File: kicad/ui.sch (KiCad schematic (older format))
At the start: 13 parts, among them J1401 NHD-4.3-480272FT-CTXL-T, J1402 Conn_01x02, U1401 PAM8301

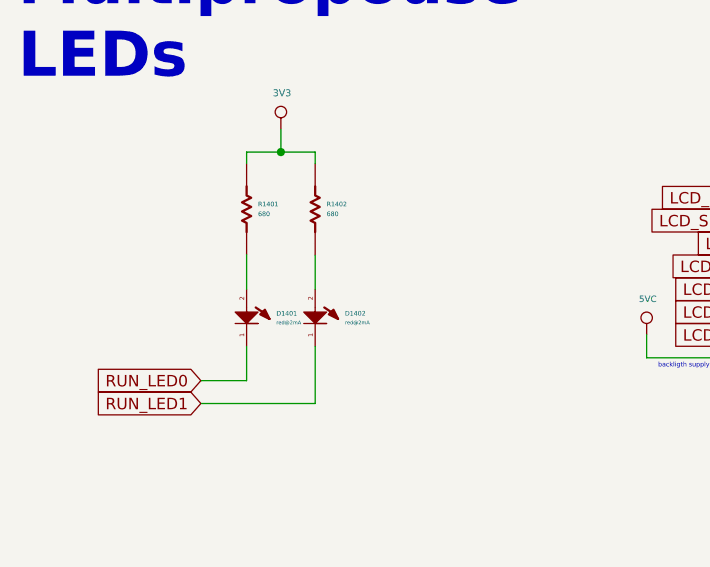
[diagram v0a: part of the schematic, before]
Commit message: making some nets space
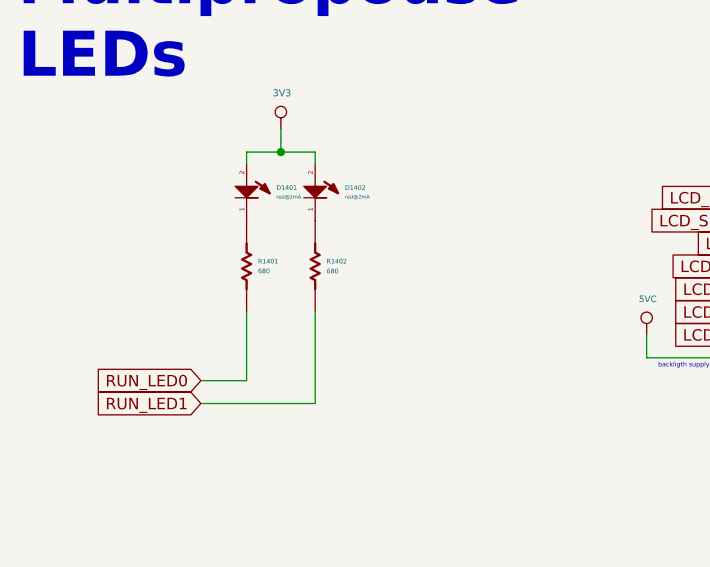
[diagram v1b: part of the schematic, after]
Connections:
- wire segments 65 -> 63
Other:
- moved on the sheet: D1401, D1402, R1401, R1402
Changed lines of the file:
@@
 	1    0    0    -1
 $EndComp
-Wire Wire Line
-	2650 2150 2650 2000
-Wire Wire Line
-	2350 2000 2350 2150
-Wire Wire Line
-	2650 2650 2650 2400
 Text Notes 1350 1250 0    197  ~ 39
 Multipropouse\nLEDs
@@
 L servo:LED_A2_K1 D?
 U 1 1 5DB38F6A
-P 2650 2250
+P 2650 1700
 AR Path="/5DD4DF4C/5DB38F6A" Ref="D?"  Part="1"
 AR Path="/5E0D58C4/5DB38F6A" Ref="D?"  Part="1"
 AR Path="/5E72D841/5DB38F6A" Ref="D1402"  Part="1"
-F 0 "D1402" V 2656 2380 20  0000 L CNN
-F 1 "red@2mA" V 2696 2380 16  0000 L CNN
-F 2 "servo:LED_0603_1608Metric" H 2450 2050 60  0001 C CNN
-F 3 "" H 2450 2050 60  0001 C CNN
-F 4 "Red" V -6350 2450 60  0001 C CNN "VALUE"
-	1    2650 2250
+F 0 "D1402" V 2656 1830 20  0000 L CNN
+F 1 "red@2mA" V 2696 1830 16  0000 L CNN
+F 2 "servo:LED_0603_1608Metric" H 2450 1500 60  0001 C CNN
+F 3 "" H 2450 1500 60  0001 C CNN
+F 4 "Red" V -6350 1900 60  0001 C CNN "VALUE"
+	1    2650 1700
 	0    1    1    0
 $EndComp
@@
 L servo:Resistor R?
 U 1 1 5DB38F5F
-P 2350 1800
+P 2350 2050
 AR Path="/5DD4DF4C/5DB38F5F" Ref="R?"  Part="1"
 AR Path="/5E0D58C4/5DB38F5F" Ref="R?"  Part="1"
 AR Path="/5E72D841/5DB38F5F" Ref="R1401"  Part="1"
-F 0 "R1401" V 2328 1850 20  0000 L CNN
-F 1 "680" V 2371 1850 20  0000 L CNN
-F 2 "Resistor_SMD:R_0603_1608Metric" H 1850 1700 60  0001 C CNN
-F 3 "" H 1950 1800 60  0001 C CNN
-F 4 "680" V -6050 2600 60  0001 C CNN "ValueDisplayed"
-	1    2350 1800
+F 0 "R1401" V 2328 2100 20  0000 L CNN
+F 1 "680" V 2371 2100 20  0000 L CNN
+F 2 "Resistor_SMD:R_0603_1608Metric" H 1850 1950 60  0001 C CNN
+F 3 "" H 1950 2050 60  0001 C CNN
+F 4 "680" V -6050 2850 60  0001 C CNN "ValueDisplayed"
+	1    2350 2050
 	0    1    1    0
 $EndComp
@@
 L servo:Resistor R?
 U 1 1 5E170B1F
-P 2650 1800
+P 2650 2050
 AR Path="/5DD4DF4C/5E170B1F" Ref="R?"  Part="1"
 AR Path="/5E0D58C4/5E170B1F" Ref="R?"  Part="1"
 AR Path="/5E72D841/5E170B1F" Ref="R1402"  Part="1"
-F 0 "R1402" V 2628 1850 20  0000 L CNN
-F 1 "680" V 2671 1850 20  0000 L CNN
-F 2 "Resistor_SMD:R_0603_1608Metric" H 2150 1700 60  0001 C CNN
-F 3 "" H 2250 1800 60  0001 C CNN
-F 4 "680" V -6350 2600 60  0001 C CNN "ValueDisplayed"
-	1    2650 1800
+F 0 "R1402" V 2628 2100 20  0000 L CNN
+F 1 "680" V 2671 2100 20  0000 L CNN
+F 2 "Resistor_SMD:R_0603_1608Metric" H 2150 1950 60  0001 C CNN
+F 3 "" H 2250 2050 60  0001 C CNN
+F 4 "680" V -6350 2850 60  0001 C CNN "ValueDisplayed"
+	1    2650 2050
 	0    1    1    0
 $EndComp
@@
 L servo:LED_A2_K1 D?
 U 1 1 5DB38F35
-P 2350 2250
+P 2350 1700
 AR Path="/5DD4DF4C/5DB38F35" Ref="D?"  Part="1"
 AR Path="/5E0D58C4/5DB38F35" Ref="D?"  Part="1"
 AR Path="/5E72D841/5DB38F35" Ref="D1401"  Part="1"
-F 0 "D1401" V 2356 2380 20  0000 L CNN
-F 1 "red@2mA" V 2396 2380 16  0000 L CNN
-F 2 "servo:LED_0603_1608Metric" H 2150 2050 60  0001 C CNN
-F 3 "" H 2150 2050 60  0001 C CNN
-F 4 "Red" V -6050 2450 60  0001 C CNN "VALUE"
-	1    2350 2250
+F 0 "D1401" V 2356 1830 20  0000 L CNN
+F 1 "red@2mA" V 2396 1830 16  0000 L CNN
+F 2 "servo:LED_0603_1608Metric" H 2150 1500 60  0001 C CNN
+F 3 "" H 2150 1500 60  0001 C CNN
+F 4 "Red" V -6050 1900 60  0001 C CNN "VALUE"
+	1    2350 1700
 	0    1    1    0
 $EndComp
@@
 Wire Wire Line
 	2500 1450 2500 1550
-Wire Wire Line
-	2350 2400 2350 2550
 $Comp
 L servo:PAM8301 U1401
@@
 Text Label 9200 1850 0    20   ~ 0
 speaker-
+Wire Wire Line
+	2650 2250 2650 2650
+Wire Wire Line
+	2350 2250 2350 2550
 $EndSCHEMATC

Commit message: change in 5v interface scenario.. remove bridges
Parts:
- removed N1401: Housing, servo:case, symbol Mechanical:Housing
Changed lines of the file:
@@
 $Descr A4 11693 8268
 encoding utf-8
-Sheet 14 19
+Sheet 14 20
 Title "clk"
 Date "2020-01-09"
@@
 Wire Wire Line
 	7900 1000 8600 1000
-$Comp
-L Mechanical:Housing N1401
-U 1 1 5E32F2AD
-P 4150 4150
-F 0 "N1401" H 4303 4184 50  0000 L CNN
-F 1 "Housing" H 4303 4093 50  0000 L CNN
-F 2 "servo:case" H 4200 4200 50  0001 C CNN
-F 3 "~" H 4200 4200 50  0001 C CNN
-	1    4150 4150
-	1    0    0    -1
-$EndComp
 Text Label 9200 1750 0    20   ~ 0
 speaker+

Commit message: serigrafia...
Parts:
- R1401, R1402, R1403, R1404: footprint Resistor_SMD:R_0603_1608Metric -> servo:R_0603_1608Metric
- U1401: footprint Package_TO_SOT_SMD:SOT-23-6 -> servo:SOT-23-6
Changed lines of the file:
@@
 F 0 "R1401" V 2328 2100 20  0000 L CNN
 F 1 "680" V 2371 2100 20  0000 L CNN
-F 2 "Resistor_SMD:R_0603_1608Metric" H 1850 1950 60  0001 C CNN
+F 2 "servo:R_0603_1608Metric" H 1850 1950 60  0001 C CNN
 F 3 "" H 1950 2050 60  0001 C CNN
 F 4 "680" V -6050 2850 60  0001 C CNN "ValueDisplayed"
@@
 F 0 "R1402" V 2628 2100 20  0000 L CNN
 F 1 "680" V 2671 2100 20  0000 L CNN
-F 2 "Resistor_SMD:R_0603_1608Metric" H 2150 1950 60  0001 C CNN
+F 2 "servo:R_0603_1608Metric" H 2150 1950 60  0001 C CNN
 F 3 "" H 2250 2050 60  0001 C CNN
 F 4 "680" V -6350 2850 60  0001 C CNN "ValueDisplayed"
@@
 F 0 "U1401" H 8800 2150 39  0000 C CNN
 F 1 "PAM8301" H 8800 2050 39  0000 C CNN
-F 2 "Package_TO_SOT_SMD:SOT-23-6" H 8600 1800 50  0001 C CNN
+F 2 "servo:SOT-23-6" H 8600 1800 50  0001 C CNN
 F 3 "https://www.diodes.com/assets/Datasheets/PAM8301.pdf" H 8600 1800 50  0001 C CNN
 	1    8600 1800
@@
 F 0 "R1403" H 7300 1815 20  0000 C CNN
 F 1 "680e" H 7300 1772 20  0000 C CNN
-F 2 "Resistor_SMD:R_0603_1608Metric" H 6800 1600 60  0001 C CNN
+F 2 "servo:R_0603_1608Metric" H 6800 1600 60  0001 C CNN
 F 3 "" H 6900 1700 60  0001 C CNN
 F 4 "680" V -1700 2500 60  0001 C CNN "ValueDisplayed"
@@
 F 0 "R1404" H 7700 1815 20  0000 C CNN
 F 1 "220e" H 7700 1772 20  0000 C CNN
-F 2 "Resistor_SMD:R_0603_1608Metric" H 7200 1600 60  0001 C CNN
+F 2 "servo:R_0603_1608Metric" H 7200 1600 60  0001 C CNN
 F 3 "" H 7300 1700 60  0001 C CNN
 F 4 "680" V -1300 2500 60  0001 C CNN "ValueDisplayed"

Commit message: improving tracks under uC
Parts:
- J1402: footprint Connector_Molex:Molex_KK-254_AE-6410-02A_1x02_P2.54mm_Vertical -> servo:Molex_KK-254_AE-6410-02A_1x02_P2.54mm_Vertical
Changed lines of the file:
@@
 F 0 "J1402" H 9580 1838 39  0000 L CNN
 F 1 "Conn_01x02" H 9580 1763 39  0000 L CNN
-F 2 "Connector_Molex:Molex_KK-254_AE-6410-02A_1x02_P2.54mm_Vertical" H 9500 1850 50  0001 C CNN
+F 2 "servo:Molex_KK-254_AE-6410-02A_1x02_P2.54mm_Vertical" H 9500 1850 50  0001 C CNN
 F 3 "~" H 9500 1850 50  0001 C CNN
 	1    9500 1850

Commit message: bom bom bom...
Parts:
- C1404: Description (none) -> CAP CER 1UF 10V X7R 0603; PartNumber (none) -> C0603C105K8RACTU; digikey (none) -> 399-11133-1-ND
- D1401: value red@2mA -> yellow@2mA; PartNumber (none) -> LY L29K-H1K2-26-Z; VALUE Red -> (none); digikey (none) -> 475-1196-1-ND
- D1402: PartNumber (none) -> LS L29K-G1H2-1-Z; VALUE Red -> (none); digikey (none) -> LS L29K-G1H2-1-Z
- R1401, R1402: value 680 -> 560; ValueDisplayed 680 -> (none)
- R1403: value 680e -> 680; ValueDisplayed 680 -> (none)
- R1404: value 220e -> 220; ValueDisplayed 680 -> (none)
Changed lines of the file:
@@
 F 1 "red@2mA" V 2696 1830 16  0000 L CNN
 F 2 "servo:LED_0603_1608Metric" H 2450 1500 60  0001 C CNN
-F 3 "" H 2450 1500 60  0001 C CNN
-F 4 "Red" V -6350 1900 60  0001 C CNN "VALUE"
+F 3 "../doc/datasheets/LS L29K.pdf" H 2450 1500 60  0001 C CNN
+F 4 "LS L29K-G1H2-1-Z " H 2650 1700 50  0001 C CNN "digikey"
+F 5 "LS L29K-G1H2-1-Z" H 0   0   50  0001 C CNN "PartNumber"
 	1    2650 1700
 	0    1    1    0
@@
 AR Path="/5E72D841/5DB38F5F" Ref="R1401"  Part="1"
 F 0 "R1401" V 2328 2100 20  0000 L CNN
-F 1 "680" V 2371 2100 20  0000 L CNN
+F 1 "560" V 2371 2100 20  0000 L CNN
 F 2 "servo:R_0603_1608Metric" H 1850 1950 60  0001 C CNN
 F 3 "" H 1950 2050 60  0001 C CNN
-F 4 "680" V -6050 2850 60  0001 C CNN "ValueDisplayed"
 	1    2350 2050
 	0    1    1    0
@@
 AR Path="/5E72D841/5E170B1F" Ref="R1402"  Part="1"
 F 0 "R1402" V 2628 2100 20  0000 L CNN
-F 1 "680" V 2671 2100 20  0000 L CNN
+F 1 "560" V 2671 2100 20  0000 L CNN
 F 2 "servo:R_0603_1608Metric" H 2150 1950 60  0001 C CNN
 F 3 "" H 2250 2050 60  0001 C CNN
-F 4 "680" V -6350 2850 60  0001 C CNN "ValueDisplayed"
 	1    2650 2050
 	0    1    1    0
@@
 AR Path="/5E0D58C4/5DB38F35" Ref="D?"  Part="1"
 AR Path="/5E72D841/5DB38F35" Ref="D1401"  Part="1"
-F 0 "D1401" V 2356 1830 20  0000 L CNN
-F 1 "red@2mA" V 2396 1830 16  0000 L CNN
+F 0 "D1401" V 2356 1622 20  0000 R CNN
+F 1 "yellow@2mA" V 2396 1622 16  0000 R CNN
 F 2 "servo:LED_0603_1608Metric" H 2150 1500 60  0001 C CNN
-F 3 "" H 2150 1500 60  0001 C CNN
-F 4 "Red" V -6050 1900 60  0001 C CNN "VALUE"
+F 3 "../doc/datasheets/LY L29K.pdf" H 2150 1500 60  0001 C CNN
+F 4 "475-1196-1-ND" H 2350 1700 50  0001 C CNN "digikey"
+F 5 "LY L29K-H1K2-26-Z " H 0   0   50  0001 C CNN "PartNumber"
 	1    2350 1700
 	0    1    1    0
@@
 AR Path="/5E72D841/5E351E31" Ref="R1403"  Part="1"
 F 0 "R1403" H 7300 1815 20  0000 C CNN
-F 1 "680e" H 7300 1772 20  0000 C CNN
+F 1 "680" H 7300 1772 20  0000 C CNN
 F 2 "servo:R_0603_1608Metric" H 6800 1600 60  0001 C CNN
 F 3 "" H 6900 1700 60  0001 C CNN
-F 4 "680" V -1700 2500 60  0001 C CNN "ValueDisplayed"
 	1    7300 1700
 	1    0    0    -1
@@
 AR Path="/5E72D841/5E352492" Ref="R1404"  Part="1"
 F 0 "R1404" H 7700 1815 20  0000 C CNN
-F 1 "220e" H 7700 1772 20  0000 C CNN
+F 1 "220" H 7700 1772 20  0000 C CNN
 F 2 "servo:R_0603_1608Metric" H 7200 1600 60  0001 C CNN
 F 3 "" H 7300 1700 60  0001 C CNN
-F 4 "680" V -1300 2500 60  0001 C CNN "ValueDisplayed"
 	1    7700 1700
 	1    0    0    -1
@@
 F 2 "servo:C_0603_1608Metric" H 8100 1600 60  0001 C CNN
 F 3 "" H 8100 1700 60  0000 C CNN
+F 4 "CAP CER 1UF 10V X7R 0603" H 0   0   50  0001 C CNN "Description"
+F 5 "" H 0   0   50  0001 C CNN "Mfr part number"
+F 6 "399-11133-1-ND" H 0   0   50  0001 C CNN "digikey"
+F 7 "C0603C105K8RACTU" H 0   0   50  0001 C CNN "PartNumber"
 	1    8100 1700
 	-1   0    0    1

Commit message: more bom...
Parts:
- C1401: Description (none) -> CAP CER 1000PF 16V X7R 0603; PartNumber (none) -> 0603B102K160CT; digikey (none) -> 1292-1378-1-ND
- C1403: value 10u -> 10uF; Description (none) -> 10µF ±20% 10V Ceramic Capacitor X5R 0603 (1608 Metric); PartNumber (none) -> GRM188R61A106ME69D; digikey (none) -> 490-10475-1-ND
- D1401: Description (none) -> LED YELLOW DIFFUSED 0603 SMD
- D1402: Description (none) -> LED RED DIFFUSED 0603 SMD
- J1401: value NHD-4.3-480272FT-CTXL-T -> idc2x10; Description (none) -> Connector Header Surface Mount 20 position 0.100\" (2.54mm); PartNumber (none) -> SBH11-NBPC-D10-SM-BK; digikey (none) -> S9188-ND; price@10 (none) -> 4.42400
- J1402: value Conn_01x02 -> header 1x2 2.54 molex; Description (none) -> Connector Header Through Hole 2 position 0.100\" (2.54mm); PartNumber (none) -> 0022232023; digikey (none) -> WM19468-ND; price@10 (none) -> 0.23100
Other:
- note added: "interfase directly using 20 wires flat cable\n for NHD-4.3-480272FT-CTXL-T newheaven LCD\nor hand wiring\nEA eDIP128B-6LWTP\nor using any paralel 8080 3v3 interfase bitbanging \nthe SPI and GPIO pins"
- note removed: "interfase directly using f20 wires flat cable\n for NHD-4.3-480272FT-CTXL-T newheaven LCD\nor hand wiring\nEA eDIP128B-6LWTP\nor using any paralel 8080 3v3 interfase bitbanging \nthe SPI and GPIO pins"
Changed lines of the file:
@@
 F 4 "LS L29K-G1H2-1-Z " H 2650 1700 50  0001 C CNN "digikey"
 F 5 "LS L29K-G1H2-1-Z" H 0   0   50  0001 C CNN "PartNumber"
+F 6 "LED RED DIFFUSED 0603 SMD " H 0   0   50  0001 C CNN "Description"
 	1    2650 1700
 	0    1    1    0
@@
 F 4 "475-1196-1-ND" H 2350 1700 50  0001 C CNN "digikey"
 F 5 "LY L29K-H1K2-26-Z " H 0   0   50  0001 C CNN "PartNumber"
+F 6 "LED YELLOW DIFFUSED 0603 SMD " H 0   0   50  0001 C CNN "Description"
 	1    2350 1700
 	0    1    1    0
@@
 F 2 "servo:C_0603_1608Metric" H 7500 1800 60  0001 C CNN
 F 3 "" H 7500 1900 60  0000 C CNN
+F 4 "CAP CER 1000PF 16V X7R 0603 " H 0   0   50  0001 C CNN "Description"
+F 5 "0603B102K160CT" H 0   0   50  0001 C CNN "PartNumber"
+F 6 "1292-1378-1-ND " H 0   0   50  0001 C CNN "digikey"
 	1    7500 1900
 	0    1    1    0
@@
 LCD UI interfase
 Text Notes 4650 3200 0    39   ~ 8
-interfase directly using f20 wires flat cable\n for NHD-4.3-480272FT-CTXL-T newheaven LCD\nor hand wiring\nEA eDIP128B-6LWTP\nor using any paralel 8080 3v3 interfase bitbanging \nthe SPI and GPIO pins
+interfase directly using 20 wires flat cable\n for NHD-4.3-480272FT-CTXL-T newheaven LCD\nor hand wiring\nEA eDIP128B-6LWTP\nor using any paralel 8080 3v3 interfase bitbanging \nthe SPI and GPIO pins
 $Comp
 L servo:5VC #PWR01405
@@
 P 5150 2050
 F 0 "J1401" H 5200 2651 50  0000 C CNN
-F 1 "NHD-4.3-480272FT-CTXL-T" H 5200 2568 39  0000 C CNN
+F 1 "idc2x10" H 5200 2568 39  0000 C CNN
 F 2 "servo:idc2x10_smd" H 5150 2050 50  0001 C CNN
 F 3 "../doc/datasheets/NHD-4.3-480272FT-CTXL-T.pdf" H 5200 2550 50  0001 C CNN
+F 4 " Connector Header Surface Mount 20 position 0.100\" (2.54mm) " H 0   0   50  0001 C CNN "Description"
+F 5 "SBH11-NBPC-D10-SM-BK" H 0   0   50  0001 C CNN "PartNumber"
+F 6 "S9188-ND" H 0   0   50  0001 C CNN "digikey"
+F 7 "4.42400" H 0   0   50  0001 C CNN "price@10"
 	1    5150 2050
 	1    0    0    -1
@@
 AR Path="/5E72D841/618DDB4B" Ref="C1403"  Part="1"
 F 0 "C1403" V 7972 1090 20  0000 R CNN
-F 1 "10u" V 7929 1090 20  0000 R CNN
+F 1 "10uF" V 7929 1090 20  0000 R CNN
 F 2 "servo:C_0603_1608Metric" H 7900 1100 60  0001 C CNN
 F 3 "" H 7900 1200 60  0000 C CNN
+F 4 "10µF ±20% 10V Ceramic Capacitor X5R 0603 (1608 Metric) " H 0   0   50  0001 C CNN "Description"
+F 5 "GRM188R61A106ME69D " H 0   0   50  0001 C CNN "PartNumber"
+F 6 "490-10475-1-ND" H 0   0   50  0001 C CNN "digikey"
 	1    7900 1200
 	0    -1   -1   0
@@
 P 9500 1850
 F 0 "J1402" H 9580 1838 39  0000 L CNN
-F 1 "Conn_01x02" H 9580 1763 39  0000 L CNN
+F 1 "header 1x2 2.54 molex" H 9580 1763 39  0000 L CNN
 F 2 "servo:Molex_KK-254_AE-6410-02A_1x02_P2.54mm_Vertical" H 9500 1850 50  0001 C CNN
-F 3 "~" H 9500 1850 50  0001 C CNN
+F 3 "" H 9500 1850 50  0001 C CNN
+F 4 "Connector Header Through Hole 2 position 0.100\" (2.54mm) " H 0   0   50  0001 C CNN "Description"
+F 5 "0022232023 " H 0   0   50  0001 C CNN "PartNumber"
+F 6 " WM19468-ND " H 0   0   50  0001 C CNN "digikey"
+F 7 "0.23100" H 0   0   50  0001 C CNN "price@10"
 	1    9500 1850
 	1    0    0    1

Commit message: stackup
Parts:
- C1401: price@10 (none) -> 0.04100
- C1403: value 10uF -> 47Uf; Description 10µF ±20% 10V Ceramic Capacitor X5R 0603 (1608 Metric) -> 47µF ±20% 6.3V Ceramic Capacitor X5R 0603 (1608 Metric); PartNumber GRM188R61A106ME69D -> GRM188R60J476ME15D; digikey 490-10475-1-ND -> 490-13247-6-ND; price@10 (none) -> 0.46900
- C1404: value 1uF -> 47Uf; Description CAP CER 1UF 10V X7R 0603 -> 47µF ±20% 6.3V Ceramic Capacitor X5R 0603 (1608 Metric); PartNumber C0603C105K8RACTU -> GRM188R60J476ME15D; digikey 399-11133-1-ND -> 490-13247-6-ND; price@10 (none) -> 0.46900
- D1401: price@10 (none) -> 0.30100
- D1402: digikey LS L29K-G1H2-1-Z -> 475-3124-1-ND; price@10 (none) -> 0.33900
- U1401: Description (none) -> Amplifier IC 1-Channel (Mono) Class D SOT-23-6; PartNumber (none) -> PAM8301AAF; digikey (none) -> PAM8301AAFDICT-ND; price@10 (none) -> 0.46800
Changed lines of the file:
@@
 F 2 "servo:LED_0603_1608Metric" H 2450 1500 60  0001 C CNN
 F 3 "../doc/datasheets/LS L29K.pdf" H 2450 1500 60  0001 C CNN
-F 4 "LS L29K-G1H2-1-Z " H 2650 1700 50  0001 C CNN "digikey"
+F 4 "475-3124-1-ND" H 2650 1700 50  0001 C CNN "digikey"
 F 5 "LS L29K-G1H2-1-Z" H 0   0   50  0001 C CNN "PartNumber"
 F 6 "LED RED DIFFUSED 0603 SMD " H 0   0   50  0001 C CNN "Description"
+F 7 "0.33900" H 0   0   50  0001 C CNN "price@10"
 	1    2650 1700
 	0    1    1    0
@@
 F 5 "LY L29K-H1K2-26-Z " H 0   0   50  0001 C CNN "PartNumber"
 F 6 "LED YELLOW DIFFUSED 0603 SMD " H 0   0   50  0001 C CNN "Description"
+F 7 "0.30100" H 0   0   50  0001 C CNN "price@10"
 	1    2350 1700
 	0    1    1    0
@@
 F 2 "servo:SOT-23-6" H 8600 1800 50  0001 C CNN
 F 3 "https://www.diodes.com/assets/Datasheets/PAM8301.pdf" H 8600 1800 50  0001 C CNN
+F 4 "Amplifier IC 1-Channel (Mono) Class D SOT-23-6" H 0   0   50  0001 C CNN "Description"
+F 5 "PAM8301AAF" H 0   0   50  0001 C CNN "PartNumber"
+F 6 "PAM8301AAFDICT-ND " H 0   0   50  0001 C CNN "digikey"
+F 7 "0.46800" H 0   0   50  0001 C CNN "price@10"
 	1    8600 1800
 	1    0    0    -1
@@
 F 5 "0603B102K160CT" H 0   0   50  0001 C CNN "PartNumber"
 F 6 "1292-1378-1-ND " H 0   0   50  0001 C CNN "digikey"
+F 7 "0.04100" H 0   0   50  0001 C CNN "price@10"
 	1    7500 1900
 	0    1    1    0
@@
 AR Path="/5E72D841/5E3524D7" Ref="C1404"  Part="1"
 F 0 "C1404" H 8150 1525 20  0000 C CNN
-F 1 "1uF" H 8150 1568 20  0000 C CNN
+F 1 "47Uf" H 8150 1568 20  0000 C CNN
 F 2 "servo:C_0603_1608Metric" H 8100 1600 60  0001 C CNN
 F 3 "" H 8100 1700 60  0000 C CNN
-F 4 "CAP CER 1UF 10V X7R 0603" H 0   0   50  0001 C CNN "Description"
-F 5 "" H 0   0   50  0001 C CNN "Mfr part number"
-F 6 "399-11133-1-ND" H 0   0   50  0001 C CNN "digikey"
-F 7 "C0603C105K8RACTU" H 0   0   50  0001 C CNN "PartNumber"
+F 4 "47µF ±20% 6.3V Ceramic Capacitor X5R 0603 (1608 Metric) " H 0   0   50  0001 C CNN "Description"
+F 5 "490-13247-6-ND" H 0   0   50  0001 C CNN "digikey"
+F 6 "GRM188R60J476ME15D" H 0   0   50  0001 C CNN "PartNumber"
+F 7 "0.46900" H 0   0   50  0001 C CNN "price@10"
 	1    8100 1700
 	-1   0    0    1
@@
 AR Path="/5E72D841/618DDB4B" Ref="C1403"  Part="1"
 F 0 "C1403" V 7972 1090 20  0000 R CNN
-F 1 "10uF" V 7929 1090 20  0000 R CNN
+F 1 "47Uf" V 7929 1090 20  0000 R CNN
 F 2 "servo:C_0603_1608Metric" H 7900 1100 60  0001 C CNN
 F 3 "" H 7900 1200 60  0000 C CNN
-F 4 "10µF ±20% 10V Ceramic Capacitor X5R 0603 (1608 Metric) " H 0   0   50  0001 C CNN "Description"
-F 5 "GRM188R61A106ME69D " H 0   0   50  0001 C CNN "PartNumber"
-F 6 "490-10475-1-ND" H 0   0   50  0001 C CNN "digikey"
+F 4 "47µF ±20% 6.3V Ceramic Capacitor X5R 0603 (1608 Metric) " H 0   0   50  0001 C CNN "Description"
+F 5 "GRM188R60J476ME15D" H 0   0   50  0001 C CNN "PartNumber"
+F 6 "490-13247-6-ND" H 0   0   50  0001 C CNN "digikey"
+F 7 "0.46900" H 0   0   50  0001 C CNN "price@10"
 	1    7900 1200
 	0    -1   -1   0

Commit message: bom copleted
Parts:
- R1401, R1402: Description (none) -> 560 Ohms ±5% 0.1W, 1/10W Chip Resistor 0603 (1608 Metric) M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; PartNumber (none) -> CR0603-JW-561ELF; digikey (none) -> 118-CR0603-JW-561ELFCT-ND; price@10 (none) -> 0.02600
- R1403: Description (none) -> 680 Ohms ±5% 0.1W, 1/10W Chip Resistor 0603 (1608 Metric) A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; PartNumber (none) -> RMCF0603JT680R; digikey (none) -> RMCF0603JT680RCT-ND; price@10 (none) -> 0.01400
- R1404: Description (none) -> 220 Ohms ±5% 0.25W, 1/4W Chip Resistor 0603 (1608 Metric) A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; PartNumber (none) -> ESR03EZPJ221; digikey (none) -> RHM220DCT-ND; price@10 (none) -> 0.07900
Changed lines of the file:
@@
 F 2 "servo:R_0603_1608Metric" H 1850 1950 60  0001 C CNN
 F 3 "" H 1950 2050 60  0001 C CNN
+F 4 "560 Ohms ±5% 0.1W, 1/10W Chip Resistor 0603 (1608 Metric) Moisture Resistant Thick Film " H 0   0   50  0001 C CNN "Description"
+F 5 "CR0603-JW-561ELF" H 0   0   50  0001 C CNN "PartNumber"
+F 6 "118-CR0603-JW-561ELFCT-ND" H 0   0   50  0001 C CNN "digikey"
+F 7 "0.02600" H 0   0   50  0001 C CNN "price@10"
 	1    2350 2050
 	0    1    1    0
@@
 F 2 "servo:R_0603_1608Metric" H 2150 1950 60  0001 C CNN
 F 3 "" H 2250 2050 60  0001 C CNN
+F 4 "560 Ohms ±5% 0.1W, 1/10W Chip Resistor 0603 (1608 Metric) Moisture Resistant Thick Film " H 0   0   50  0001 C CNN "Description"
+F 5 "CR0603-JW-561ELF" H 0   0   50  0001 C CNN "PartNumber"
+F 6 "118-CR0603-JW-561ELFCT-ND" H 0   0   50  0001 C CNN "digikey"
+F 7 "0.02600" H 0   0   50  0001 C CNN "price@10"
 	1    2650 2050
 	0    1    1    0
@@
 F 2 "servo:R_0603_1608Metric" H 6800 1600 60  0001 C CNN
 F 3 "" H 6900 1700 60  0001 C CNN
+F 4 "680 Ohms ±5% 0.1W, 1/10W Chip Resistor 0603 (1608 Metric) Automotive AEC-Q200 Thick Film" H 0   0   50  0001 C CNN "Description"
+F 5 "RMCF0603JT680R" H 0   0   50  0001 C CNN "PartNumber"
+F 6 "RMCF0603JT680RCT-ND" H 0   0   50  0001 C CNN "digikey"
+F 7 "0.01400" H 0   0   50  0001 C CNN "price@10"
 	1    7300 1700
 	1    0    0    -1
@@
 F 2 "servo:R_0603_1608Metric" H 7200 1600 60  0001 C CNN
 F 3 "" H 7300 1700 60  0001 C CNN
+F 4 "220 Ohms ±5% 0.25W, 1/4W Chip Resistor 0603 (1608 Metric) Automotive AEC-Q200, Pulse Withstanding Thick Film " H 0   0   50  0001 C CNN "Description"
+F 5 "ESR03EZPJ221" H 0   0   50  0001 C CNN "PartNumber"
+F 6 "RHM220DCT-ND" H 0   0   50  0001 C CNN "digikey"
+F 7 "0.07900" H 0   0   50  0001 C CNN "price@10"
 	1    7700 1700
 	1    0    0    -1
